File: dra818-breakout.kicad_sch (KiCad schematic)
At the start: 4 parts, among them J1 Conn_01x06, J2 Conn_01x05, U1 DRA818V

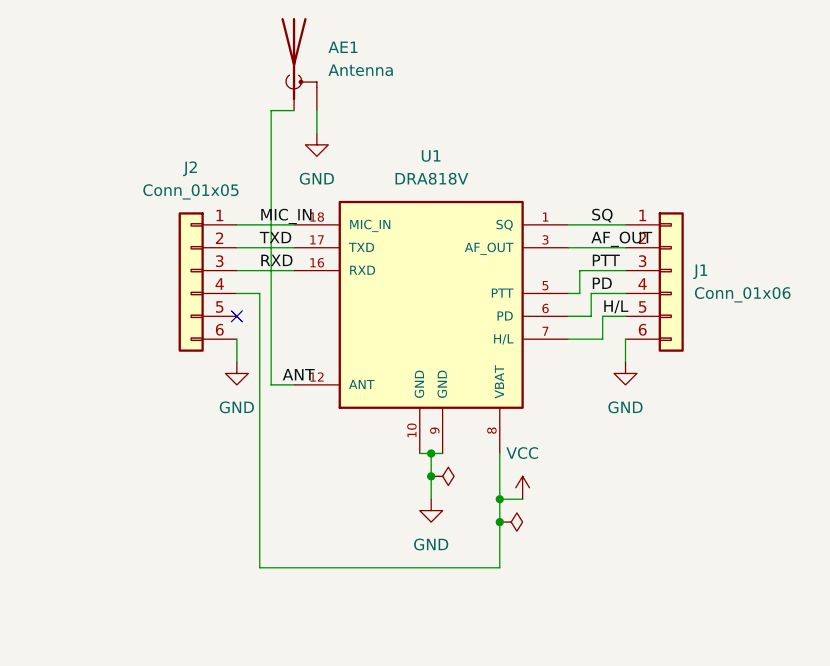
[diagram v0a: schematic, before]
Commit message: More detail for publishing
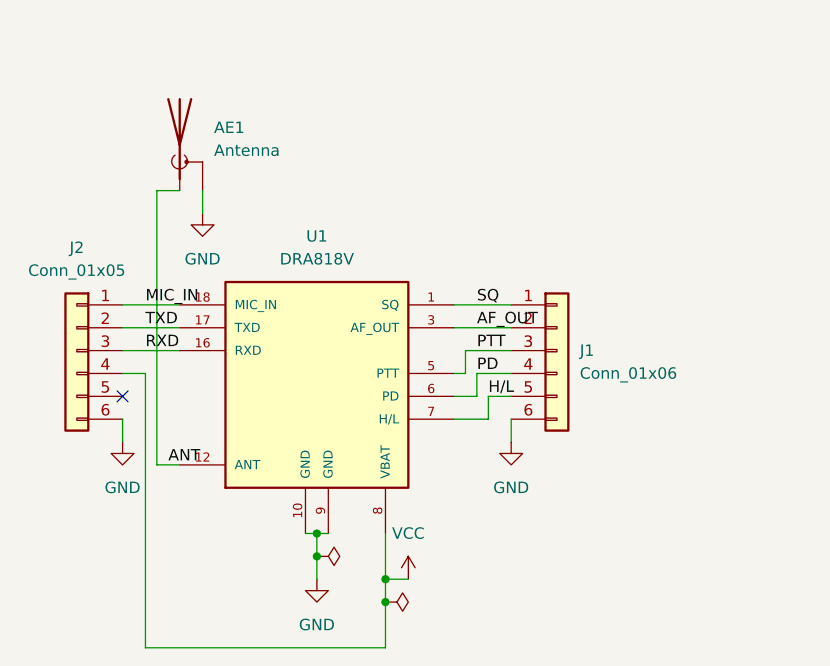
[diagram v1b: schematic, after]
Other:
- company: (none) -> C Keller K0SWE
- title: (none) -> DRA818 Breakout
- moved on the sheet: AE1, J1, J2, U1

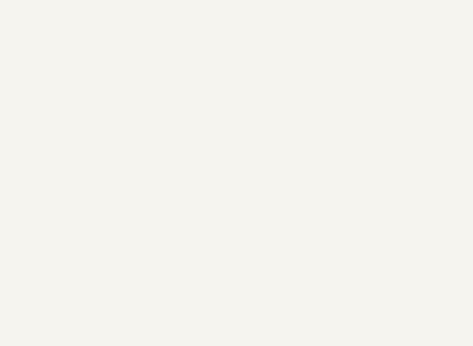
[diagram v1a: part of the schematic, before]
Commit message: Add open hardware logo
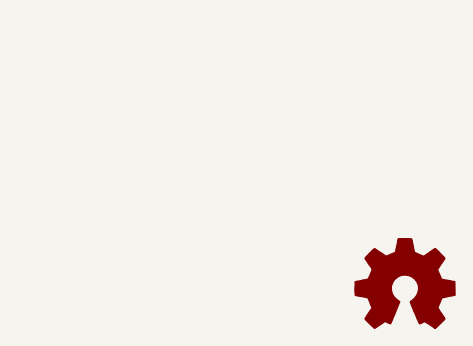
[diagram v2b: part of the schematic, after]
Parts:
- added SYM1: Logo_Open_Hardware_Small, Symbol:OSHW-Logo2_7.3x6mm_SilkScreen, symbol Graphic:Logo_Open_Hardware_Small
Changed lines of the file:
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@@
+    )
+  )
+  (symbol (lib_id "Graphic:Logo_Open_Hardware_Small") (at 257.81 180.34 0) (unit 1)
+    (in_bom no) (on_board yes) (dnp no) (fields_autoplaced)
+    (property "Reference" "SYM1" (at 257.81 173.355 0)
+      (effects (font (size 1.27 1.27)) hide)
+    )
+    (property "Value" "Logo_Open_Hardware_Small" (at 257.81 186.055 0)
+      (effects (font (size 1.27 1.27)) hide)
+    )
+    (property "Footprint" "Symbol:OSHW-Logo2_7.3x6mm_SilkScreen" (at 257.81 180.34 0)
+      (effects (font (size 1.27 1.27)) hide)
+    )
+    (property "Datasheet" "~" (at 257.81 180.34 0)
+      (effects (font (size 1.27 1.27)) hide)
+    )
+    (property "Sim.Enable" "0" (at 257.81 180.34 0)
+      (effects (font (size 1.27 1.27)) hide)
+    )
+    (instances
+      (project "dra818-breakout"
+        (path "/220fd5b7-d6b4-4f18-8941-38a06a99065a"
+          (reference "SYM1") (unit 1)
+        )
+      )
     )
   )
